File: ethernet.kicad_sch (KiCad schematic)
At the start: 37 parts, among them IC1 ACPL-217-500E, J6 5-2337992-8, U22 TPS2372-3RGWR, U23 ULS-12{slash}5-D48N-C

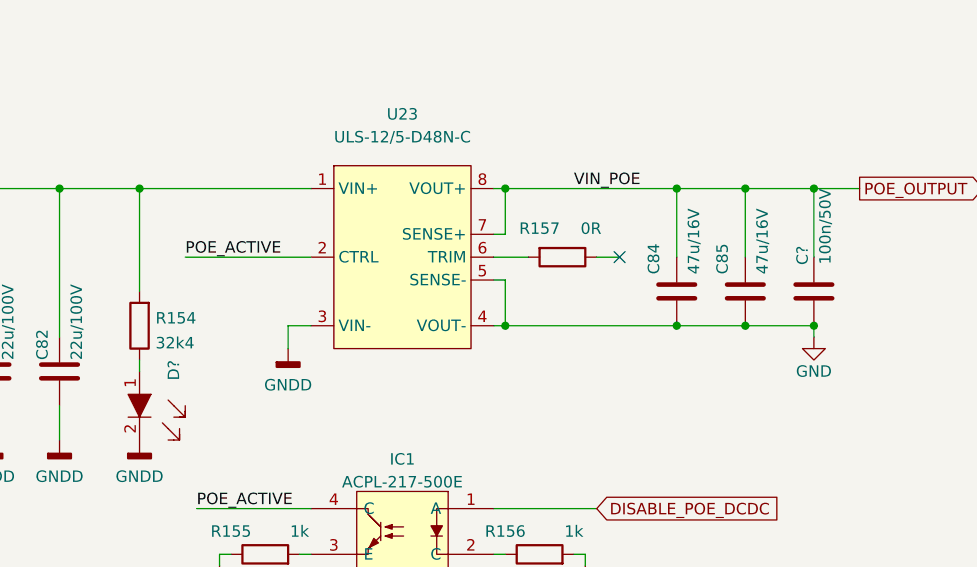
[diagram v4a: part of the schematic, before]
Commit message: Handled connection of unconnected pins and removed unnecessary labels
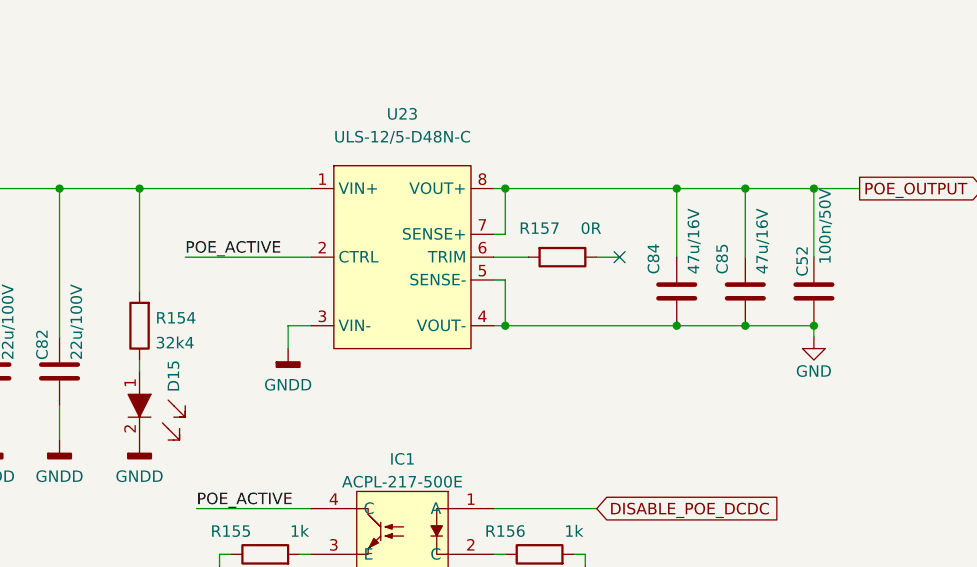
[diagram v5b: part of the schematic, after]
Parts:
- gave numbers to parts that had none: 2
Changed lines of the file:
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@@
-    (effects (font (size 1.27 1.27)) (justify left bottom))
-  )
-  (label "VIN_POE" (at 313.69 181.61 0)
     (effects (font (size 1.27 1.27)) (justify left bottom))
   )
@@
   (symbol (lib_id "antmicroCapacitorsmisc:C_100n_0402_50V") (at 340.36 193.04 0) (mirror y) (unit 1)
     (in_bom yes) (on_board yes)
-    (property "Reference" "C?" (id 0) (at 339.09 187.96 90)
+    (property "Reference" "C52" (id 0) (at 339.09 187.96 90)
       (effects (font (size 1.27 1.27)) (justify right))
     )
@@
   (symbol (lib_id "antmicroLEDIndicationDiscrete:LTST-C190GKT") (at 265.43 207.01 270) (unit 1)
     (in_bom yes) (on_board yes)
-    (property "Reference" "D?" (id 0) (at 269.24 200.66 0)
-      (effects (font (size 1.27 1.27)) (justify left))
-    )
+    (property "Reference" "D15" (id 0) (at 269.24 200.66 0)
+      (effects (font (size 1.27 1.27)) (justify left))
+    )

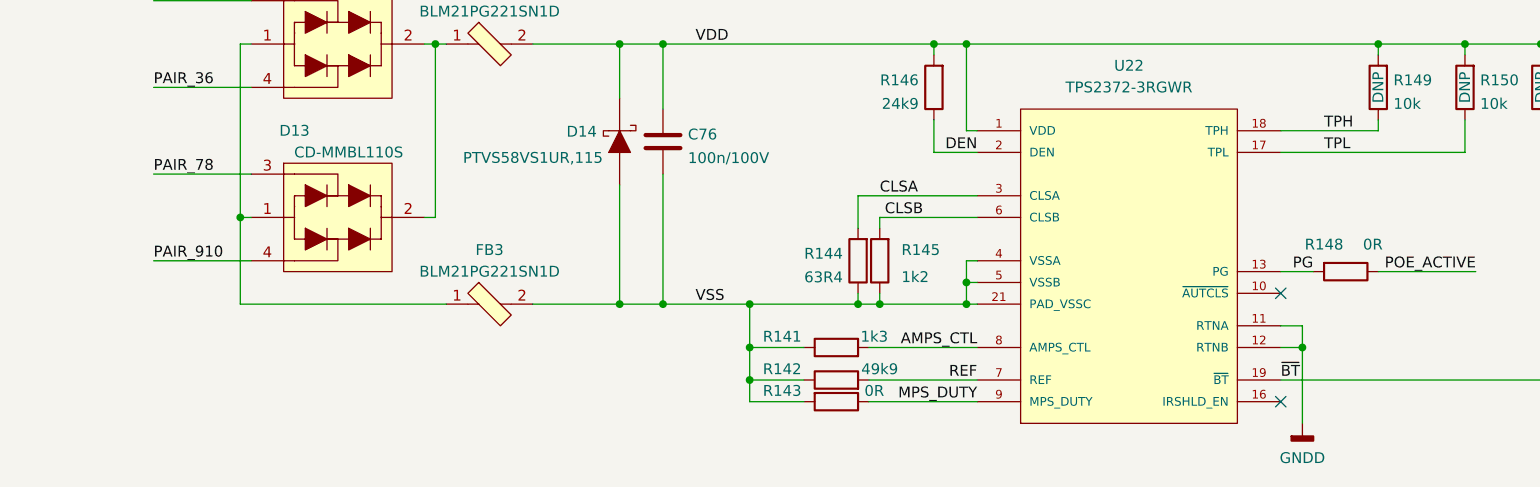
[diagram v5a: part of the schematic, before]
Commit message: Started routing PoE circuitry
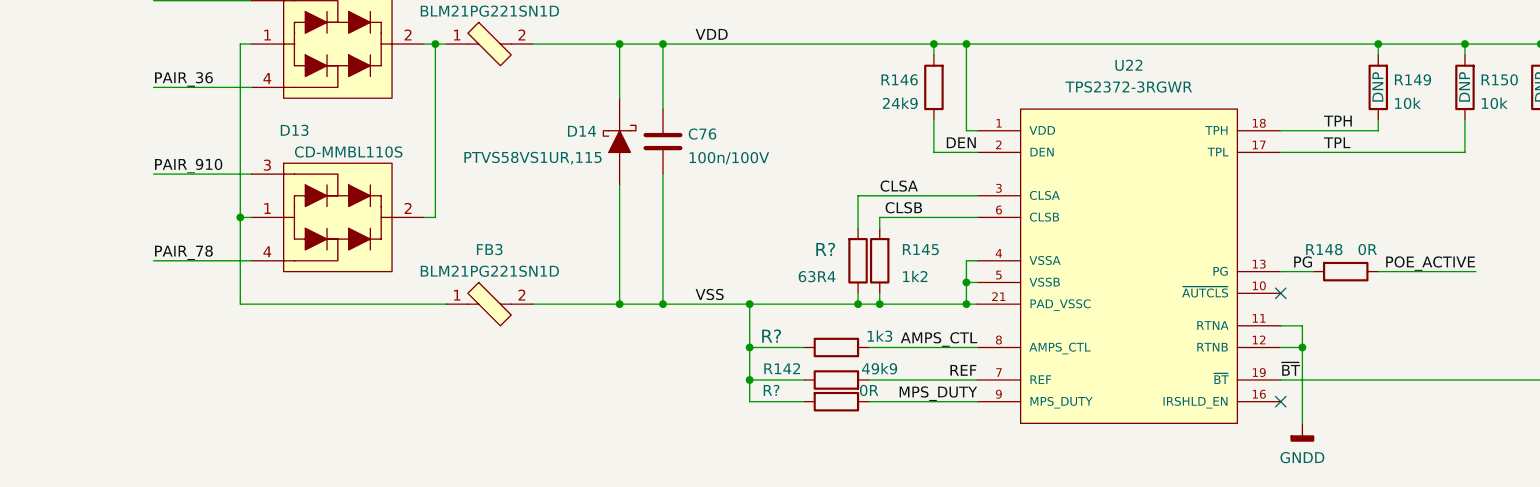
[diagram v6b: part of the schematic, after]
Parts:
- removed R141: R_1k3_0603, antmicro-footprints:0603-res, symbol antmicroResistors0603:R_1k3_0603
- removed R143: R_0R_0603, antmicro-footprints:0603-res, symbol antmicroResistors0603:R_0R_0603
- removed R144: R_63R4_0603, antmicro-footprints:0603-res, symbol antmicroResistors0603:R_63R4_0603
- added R?: R_63R4_0402, antmicro-footprints:0402-res, symbol antmicroResistors0402:R_63R4_0402
- added R?: R_0R_0402, antmicro-footprints:0402-res, symbol antmicroResistors0402:R_0R_0402
- added R?: R_1k3_0402, antmicro-footprints:0402-res, symbol antmicroResistors0402:R_1k3_0402
- R148: value R_0R_0603 -> R_0R_0402; footprint antmicro-footprints:0603-res -> antmicro-footprints:0402-res; symbol antmicroResistors0603:R_0R_0603 -> antmicroResistors0402:R_0R_0402; MPN CR0603-J/-000ELF -> ERJ2GE0R00X; Manufacturer BOURNS -> PANASONIC
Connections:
- net AMPS_CTL: now also R?.2
- net CLSA: now also R?.2
- net MPS_DUTY: now also R?.1
- net PAIR_78: now also D13.4; no longer D13.3
- net PAIR_910: now also D13.3; no longer D13.4
- net VSS: now also R?.1, R?.1, R?.2
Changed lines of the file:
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@@
     (stroke (width 0) (type default) (color 0 0 0 0))
   )
-  (wire (pts (xy 62.23 196.85) (xy 73.66 196.85))
+  (wire (pts (xy 62.23 207.01) (xy 73.66 207.01))
     (stroke (width 0) (type default) (color 0 0 0 0))
   )
@@
     (stroke (width 0) (type default) (color 0 0 0 0))
   )
-  (wire (pts (xy 62.23 207.01) (xy 73.66 207.01))
+  (wire (pts (xy 62.23 196.85) (xy 73.66 196.85))
     (stroke (width 0) (type default) (color 0 0 0 0))
   )
@@
     (stroke (width 0) (type default) (color 0 0 0 0))
   )
-  (wire (pts (xy 62.23 176.53) (xy 73.66 176.53))
+  (wire (pts (xy 62.23 186.69) (xy 73.66 186.69))
     (stroke (width 0) (type default) (color 0 0 0 0))
   )
@@
     (stroke (width 0) (type default) (color 0 0 0 0))
   )
-  (wire (pts (xy 62.23 186.69) (xy 73.66 186.69))
+  (wire (pts (xy 62.23 176.53) (xy 73.66 176.53))
     (stroke (width 0) (type default) (color 0 0 0 0))
   )
@@
     (effects (font (size 1.27 1.27)) (justify right bottom))
   )
-  (label "PAIR_910" (at 62.23 207.01 0)
+  (label "PAIR_910" (at 62.23 196.85 0)
     (effects (font (size 1.27 1.27)) (justify left bottom))
   )
@@
     (effects (font (size 1.27 1.27)) (justify left bottom))
   )
-  (label "PAIR_78" (at 62.23 196.85 0)
+  (label "PAIR_78" (at 62.23 207.01 0)
     (effects (font (size 1.27 1.27)) (justify left bottom))
   )
@@
     (pin "1")
   )
+  (symbol (lib_id "antmicroResistors0402:R_63R4_0402") (at 144.78 207.01 270) (mirror x) (unit 1)
+    (in_bom yes) (on_board yes) (fields_autoplaced)
+    (property "Reference" "R?" (id 0) (at 142.24 205.74 90)
+      (effects (font (size 1.524 1.524)) (justify right))
+    )
+    (property "Value" "R_63R4_0402" (id 1) (at 140.97 207.01 0)
+      (effects (font (size 1.524 1.524)) hide)
+    )
+    (property "Footprint" "antmicro-footprints:0402-res" (id 2) (at 149.86 201.93 0)
+      (effects (font (size 1.524 1.524)) (justify left) hide)
+    )
+    (property "Datasheet" "" (id 3) (at 144.78 207.01 0)
+      (effects (font (size 1.27 1.27)) hide)
+    )
+    (property "Manufacturer" "Vishay" (id 4) (at 154.94 201.93 0)
+      (effects (font (size 1.524 1.524)) (justify left) hide)
+    )
+    (property "MPN" "CRCW040263R4FKED" (id 5) (at 152.4 201.93 0)
+      (effects (font (size 1.524 1.524)) (justify left) hide)
+    )
+    (property "Val" "63R4" (id 6) (at 142.24 208.9149 90)
+      (effects (font (size 1.27 1.27)) (justify right))
+    )
+    (pin "1")
+    (pin "2")
+  )
+  (symbol (lib_id "antmicroResistors0402:R_0R_0402") (at 142.24 223.52 180) (unit 1)
+    (in_bom yes) (on_board yes)
+    (property "Reference" "R?" (id 0) (at 134.62 222.25 0))
+    (property "Value" "R_0R_0402" (id 1) (at 142.24 219.71 0)
+      (effects (font (size 1.524 1.524)) hide)
+    )
+    (property "Footprint" "antmicro-footprints:0402-res" (id 2) (at 137.16 228.6 0)
+      (effects (font (size 1.524 1.524)) (justify left) hide)
+    )
+    (property "Datasheet" "" (id 3) (at 142.24 223.52 0)
+      (effects (font (size 1.27 1.27)) hide)
+    )
+    (property "Manufacturer" "PANASONIC" (id 4) (at 137.16 233.68 0)
+      (effects (font (size 1.524 1.524)) (justify left) hide)
+    )
+    (property "MPN" "ERJ2GE0R00X" (id 5) (at 137.16 231.14 0)
+      (effects (font (size 1.524 1.524)) (justify left) hide)
+    )
+    (property "Val" "0R" (id 6) (at 146.05 222.25 0))
+    (pin "1")
+    (pin "2")
+  )
   (symbol (lib_name "BLM21PG221SN1D_1") (lib_id "antmicroFerriteBeadsandChips:BLM21PG221SN1D") (at 101.6 212.09 0) (unit 1)
     (in_bom yes) (on_board yes) (fields_autoplaced)
@@
     (pin "4")
   )
-  (symbol (lib_id "antmicroResistors0603:R_0R_0603") (at 201.93 208.28 180) (unit 1)
+  (symbol (lib_id "antmicroResistors0402:R_0R_0402") (at 201.93 208.28 180) (unit 1)
     (in_bom yes) (on_board yes)
-    (property "Reference" "R148" (id 0) (at 199.39 205.105 0))
-    (property "Value" "R_0R_0603" (id 1) (at 201.93 204.47 0)
-      (effects (font (size 1.27 1.27)) hide)
+    (property "Reference" "R148" (id 0) (at 199.39 205.74 0))
+    (property "Value" "R_0R_0402" (id 1) (at 201.93 204.47 0)
+      (effects (font (size 1.524 1.524)) hide)
     )
-    (property "Footprint" "antmicro-footprints:0603-res" (id 2) (at 196.85 213.36 0)
+    (property "Footprint" "antmicro-footprints:0402-res" (id 2) (at 196.85 213.36 0)
       (effects (font (size 1.524 1.524)) (justify left) hide)
     )
@@
       (effects (font (size 1.27 1.27)) hide)
     )
-    (property "Manufacturer" "BOURNS" (id 4) (at 196.85 218.44 0)
+    (property "Manufacturer" "PANASONIC" (id 4) (at 196.85 218.44 0)
       (effects (font (size 1.524 1.524)) (justify left) hide)
     )
-    (property "MPN" "CR0603-J/-000ELF" (id 5) (at 196.85 215.9 0)
+    (property "MPN" "ERJ2GE0R00X" (id 5) (at 196.85 215.9 0)
       (effects (font (size 1.524 1.524)) (justify left) hide)
     )
-    (property "Val" "0R" (id 6) (at 205.105 205.105 0))
+    (property "Val" "0R" (id 6) (at 204.47 205.74 0))
     (pin "1")
     (pin "2")
@@
     (pin "2")
   )
-  (symbol (lib_id "antmicroResistors0603:R_0R_0603") (at 142.24 223.52 180) (unit 1)
-    (in_bom yes) (on_board yes)
-    (property "Reference" "R143" (id 0) (at 135.89 222.25 0))
-    (property "Value" "R_0R_0603" (id 1) (at 142.24 219.71 0)
-      (effects (font (size 1.27 1.27)) hide)
-    )
-    (property "Footprint" "antmicro-footprints:0603-res" (id 2) (at 137.16 228.6 0)
-      (effects (font (size 1.524 1.524)) (justify left) hide)
-    )
-    (property "Datasheet" "" (id 3) (at 142.24 223.52 0)
-      (effects (font (size 1.27 1.27)) hide)
-    )
-    (property "Manufacturer" "BOURNS" (id 4) (at 137.16 233.68 0)
-      (effects (font (size 1.524 1.524)) (justify left) hide)
-    )
-    (property "MPN" "CR0603-J/-000ELF" (id 5) (at 137.16 231.14 0)
-      (effects (font (size 1.524 1.524)) (justify left) hide)
-    )
-    (property "Val" "0R" (id 6) (at 146.685 222.25 0))
-    (pin "1")
-    (pin "2")
-  )
   (symbol (lib_id "antmicroResistors0402:R_220R_0402") (at 219.71 86.36 0) (mirror x) (unit 1)
     (in_bom yes) (on_board yes)
@@
     (pin "9")
   )
-  (symbol (lib_id "antmicroResistors0603:R_1k3_0603") (at 142.24 217.17 0) (unit 1)
-    (in_bom yes) (on_board yes)
-    (property "Reference" "R141" (id 0) (at 135.89 215.9 0))
-    (property "Value" "R_1k3_0603" (id 1) (at 142.24 220.98 0)
-      (effects (font (size 1.27 1.27)) hide)
-    )
-    (property "Footprint" "antmicro-footprints:0603-res" (id 2) (at 147.32 212.09 0)
-      (effects (font (size 1.524 1.524)) (justify left) hide)
-    )
-    (property "Datasheet" "" (id 3) (at 142.24 217.17 0)
-      (effects (font (size 1.27 1.27)) hide)
-    )
-    (property "Manufacturer" "PANASONIC_ELECTRONIC_COMPONENTS" (id 4) (at 147.32 207.01 0)
-      (effects (font (size 1.524 1.524)) (justify left) hide)
-    )
-    (property "MPN" "ERJ3GEYJ132V" (id 5) (at 147.32 209.55 0)
-      (effects (font (size 1.524 1.524)) (justify left) hide)
-    )
-    (property "Val" "1k3" (id 6) (at 146.685 215.9 0))
-    (pin "1")
-    (pin "2")
-  )
   (symbol (lib_id "antmicroCapacitors0402:C_100n_0402") (at 182.88 104.14 0) (unit 1)
     (in_bom yes) (on_board yes) (fields_autoplaced)
@@
     (pin "2")
   )
-  (symbol (lib_id "antmicroResistors0603:R_63R4_0603") (at 144.78 207.01 90) (unit 1)
-    (in_bom yes) (on_board yes) (fields_autoplaced)
-    (property "Reference" "R144" (id 0) (at 143.002 206.1754 90)
-      (effects (font (size 1.27 1.27)) (justify left))
+  (symbol (lib_id "antmicroResistors0402:R_1k3_0402") (at 142.24 217.17 0) (unit 1)
+    (in_bom yes) (on_board yes)
+    (property "Reference" "R?" (id 0) (at 134.62 215.9 0)
+      (effects (font (size 1.524 1.524)))
     )
-    (property "Value" "R_63R4_0603" (id 1) (at 148.59 207.01 0)
-      (effects (font (size 1.27 1.27)) hide)
+    (property "Value" "R_1k3_0402" (id 1) (at 144.78 203.2 0)
+      (effects (font (size 1.524 1.524)) (justify left bottom) hide)
     )
-    (property "Footprint" "antmicro-footprints:0603-res" (id 2) (at 139.7 201.93 0)
+    (property "Footprint" "antmicro-footprints:0402-res" (id 2) (at 144.78 209.55 0)
       (effects (font (size 1.524 1.524)) (justify left) hide)
     )
-    (property "Datasheet" "" (id 3) (at 144.78 207.01 0)
-      (effects (font (size 1.27 1.27)) hide)
+    (property "Datasheet" "https://www.mouser.pl/datasheet/2/54/cr-1858361.pdf" (id 3) (at 144.78 213.36 0)
+      (effects (font (size 1.27 1.27)) (justify left bottom) hide)
     )
-    (property "Manufacturer" "PANASONIC" (id 4) (at 134.62 201.93 0)
+    (property "Manufacturer" "Bourns" (id 4) (at 144.78 204.47 0)
       (effects (font (size 1.524 1.524)) (justify left) hide)
     )
-    (property "MPN" "ERJPA3F63R4V" (id 5) (at 137.16 201.93 0)
+    (property "MPN" "CR0402-FX-1301GLF " (id 5) (at 144.78 207.01 0)
       (effects (font (size 1.524 1.524)) (justify left) hide)
     )
-    (property "Val" "63R4" (id 6) (at 143.002 208.9405 90)
-      (effects (font (size 1.27 1.27)) (justify left))
-    )
+    (property "Val" "1k3" (id 6) (at 147.32 215.9 0))
     (pin "1")
     (pin "2")

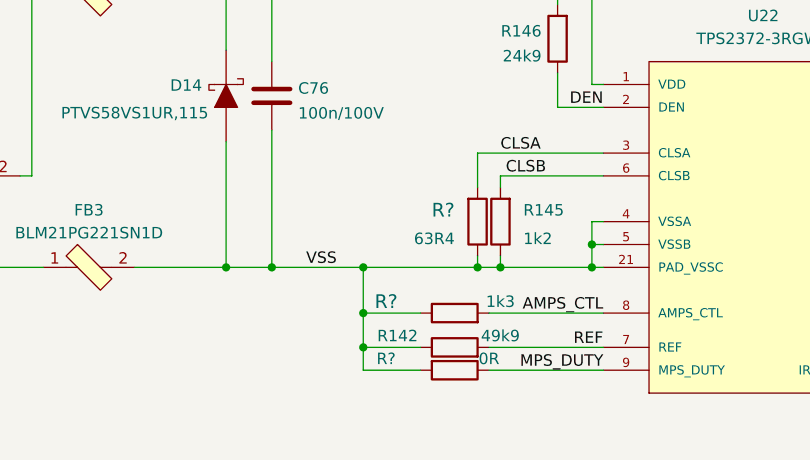
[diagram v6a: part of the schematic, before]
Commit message: Routed ethernet MDI
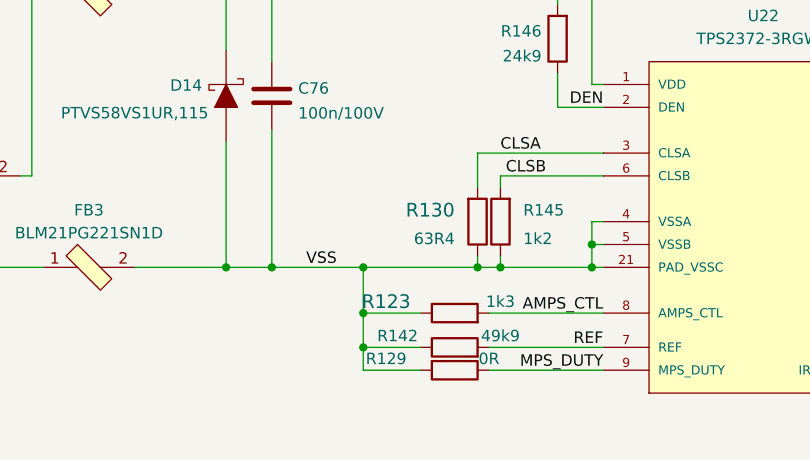
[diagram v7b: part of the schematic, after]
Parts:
- gave numbers to parts that had none: 3
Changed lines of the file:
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@@
   (symbol (lib_id "antmicroResistors0402:R_63R4_0402") (at 144.78 207.01 270) (mirror x) (unit 1)
     (in_bom yes) (on_board yes) (fields_autoplaced)
-    (property "Reference" "R?" (id 0) (at 142.24 205.74 90)
+    (property "Reference" "R130" (id 0) (at 142.24 205.74 90)
       (effects (font (size 1.524 1.524)) (justify right))
     )
@@
   (symbol (lib_id "antmicroResistors0402:R_0R_0402") (at 142.24 223.52 180) (unit 1)
     (in_bom yes) (on_board yes)
-    (property "Reference" "R?" (id 0) (at 134.62 222.25 0))
+    (property "Reference" "R129" (id 0) (at 134.62 222.25 0))
     (property "Value" "R_0R_0402" (id 1) (at 142.24 219.71 0)
       (effects (font (size 1.524 1.524)) hide)
@@
   (symbol (lib_id "antmicroResistors0402:R_1k3_0402") (at 142.24 217.17 0) (unit 1)
     (in_bom yes) (on_board yes)
-    (property "Reference" "R?" (id 0) (at 134.62 215.9 0)
+    (property "Reference" "R123" (id 0) (at 134.62 215.9 0)
       (effects (font (size 1.524 1.524)))
     )
